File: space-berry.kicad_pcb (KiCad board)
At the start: 8 copper layers, 128 parts, among them Q1 SiS415DNT, Q2 TSM2302CX, U11 RTL8211F-CG, U12 K4A8G165WC-BCTD, U13 XCZU15EG-2FFVB1156E, U14 K4A8G165WC-BCTD, U6 TLV75801PDBV, U7 TLV75801PDBV, U8 TLV75801PDBV, U9 TLV75801PDBV

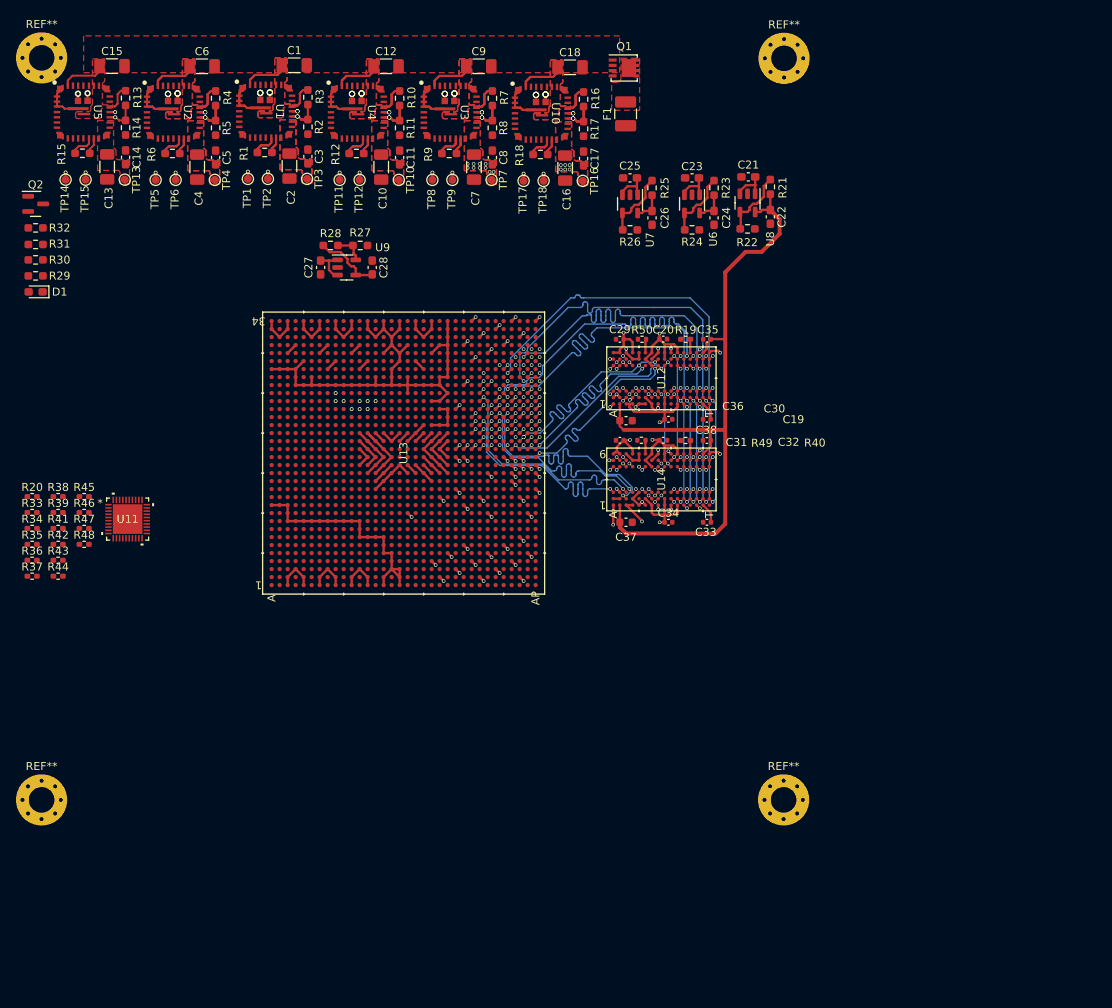
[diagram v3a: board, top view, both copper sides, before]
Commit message: Gbe routing
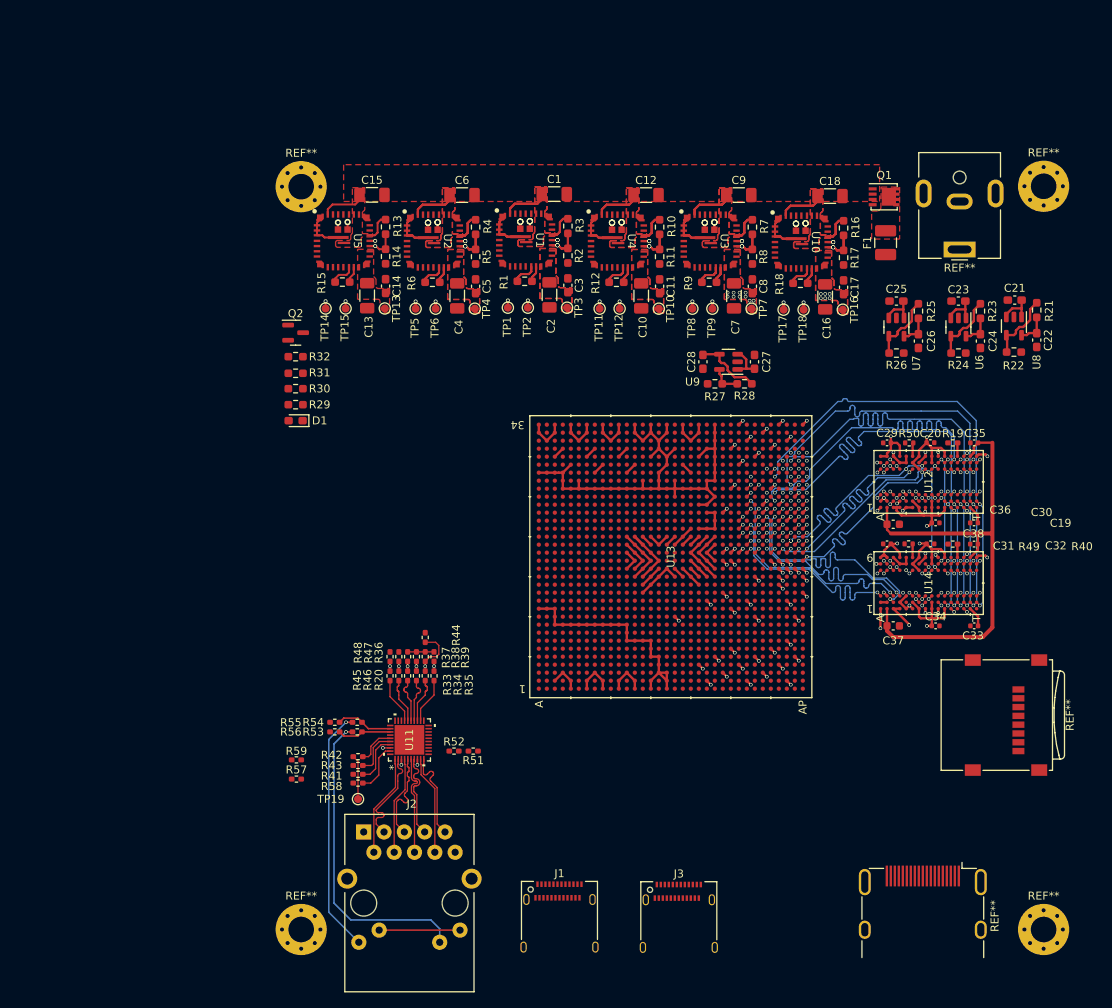
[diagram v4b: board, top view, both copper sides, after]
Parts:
- added J1: USB_C_Receptacle, Connector_USB:USB_C_Receptacle_Amphenol_12401610E4-2A, F.Cu at (127.5, 140.1)
- added J2: RJ45_RB1-125B8G1A, Connector_RJ:RJ45_UDE_RB1-125B8G1A, F.Cu at (103.0, 128.5)
- added J3: USB_C_Receptacle, Connector_USB:USB_C_Receptacle_Amphenol_12401610E4-2A, F.Cu at (142.4, 140.1)
- added R51: 22, Resistor_SMD:R_0402_1005Metric_Pad0.72x0.64mm_HandSolder, F.Cu at (116.7, 118.4)
- added R52: 4K7, Resistor_SMD:R_0402_1005Metric_Pad0.72x0.64mm_HandSolder, F.Cu at (114.3, 118.4)
- added R53: 420, Resistor_SMD:R_0402_1005Metric_Pad0.72x0.64mm_HandSolder, F.Cu at (102.2, 116.0)
- added R54: 420, Resistor_SMD:R_0402_1005Metric_Pad0.72x0.64mm_HandSolder, F.Cu at (102.2, 114.8)
- added R55: 4K7, Resistor_SMD:R_0402_1005Metric_Pad0.72x0.64mm_HandSolder, F.Cu at (99.4, 114.8)
- added R56: 4K7, Resistor_SMD:R_0402_1005Metric_Pad0.72x0.64mm_HandSolder, F.Cu at (99.4, 116.0)
- added R57: 420, Resistor_SMD:R_0402_1005Metric_Pad0.72x0.64mm_HandSolder, F.Cu at (94.6, 121.9)
- added R58: 2K5, Resistor_SMD:R_0402_1005Metric_Pad0.72x0.64mm_HandSolder, F.Cu at (102.3, 122.4)
- added R59: 4K7, Resistor_SMD:R_0402_1005Metric_Pad0.72x0.64mm_HandSolder, F.Cu at (94.6, 119.5)
- added REF**: BarrelJack_CUI_PJ-063AH_Horizontal, Connector_BarrelJack:BarrelJack_CUI_PJ-063AH_Horizontal, F.Cu at (177.5, 55.7)
- added REF**: HDMI_A_Molex_208658-1001_Horizontal, Connector_HDMI:HDMI_A_Molex_208658-1001_Horizontal, F.Cu at (172.9, 137.3)
- added REF**: microSD_HC_Wuerth_693072010801, Connector_Card:microSD_HC_Wuerth_693072010801, F.Cu at (183.3, 113.9)
- added TP19: Eth clk, TestPoint:TestPoint_Pad_D1.0mm, F.Cu at (102.3, 124.4)
- R41, R42, R43: value 4K7 -> 22
- R44: value 4K7 -> 1K
- R47, R48: value 22 -> 1K
- moved C27 55.5 mm to (151.9, 69.7), turned to 90 degrees
- moved R28 54.6 mm to (150.6, 72.5), turned to 0 degrees
- moved R35 52.9 mm to (111.8, 109.0), turned to -90 degrees
- moved R34 52.5 mm to (110.7, 109.0), turned to -90 degrees
- moved R33 52.2 mm to (109.6, 109.0), turned to -90 degrees
- moved R20 52.0 mm to (108.5, 109.0), turned to -90 degrees
- moved R36 51.7 mm to (111.8, 106.6), turned to -90 degrees
- moved R37 50.2 mm to (110.7, 106.6), turned to -90 degrees
- moved U9 49.2 mm to (148.6, 69.7), turned to 180 degrees
- moved R38 49.1 mm to (109.6, 106.6), turned to -90 degrees
- moved R41 48.5 mm to (102.3, 121.3), turned to 180 degrees
- moved R27 47.6 mm to (146.9, 72.5), turned to 0 degrees
- moved R39 47.3 mm to (108.5, 106.6), turned to -90 degrees
- moved R44 46.5 mm to (110.7, 104.2), turned to -90 degrees
- moved R42 45.9 mm to (102.3, 119.1), turned to 180 degrees
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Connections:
- R41 pad 1: 1V8_ETH -> Net-(U11A-XTAL_OUT/EXT_CLK)
- R41 pad 2: ETH_TXD3 -> ETH_CLK
- R42 pad 1: 1V8_ETH -> Net-(U11A-CLKOUT)
- R42 pad 2: ETH_TXD2 -> Net-(R42-Pad2)
- R43 pad 1: 1V8_ETH -> Net-(U11A-XTAL_IN)
- R43 pad 2: ETH_TXD1 -> GND
- R44 pad 1: 1V8_ETH -> GND
- R44 pad 2: ETH_TXD0 -> ETH_RXD2
- R45 pad 1: ETH_TXD0 -> Net-(U11A-RXC/PHYAD1)
- R45 pad 2: Net-(U11A-TXD0) -> ETH_RX_CTL
- R46 pad 1: ETH_TXD1 -> Net-(U11A-RXCTL/PHYAD2)
- R46 pad 2: Net-(U11A-TXD1) -> ETH_RX_CLK
- R47 pad 1: ETH_TXD2 -> GND
- R47 pad 2: Net-(U11A-TXD2) -> ETH_RX_CLK
- R48 pad 1: ETH_TXD3 -> GND
- R48 pad 2: Net-(U11A-TXD3) -> ETH_RX_CTL
- U11 pad 11: (no net) -> 3V3
- U11 pad 12: unconnected-(U11A-PHYRSTB-Pad12) -> Net-(U11A-PHYRSTB)
- U11 pad 15: Net-(U11A-TXD3) -> ETH_TXD3
- U11 pad 16: Net-(U11A-TXD2) -> ETH_TXD2
- U11 pad 17: Net-(U11A-TXD1) -> ETH_TXD1
- U11 pad 18: Net-(U11A-TXD0) -> ETH_TXD0
- U11 pad 19: unconnected-(U11A-TXCTL-Pad19) -> ETH_TX_CTL
- U11 pad 20: unconnected-(U11A-TXC-Pad20) -> ETH_TX_CLK
- U11 pad 21: (no net) -> unconnected-(U11B-DVDD10-Pad21)
- U11 pad 26: unconnected-(U11A-RXCTL/PHYAD2-Pad26) -> Net-(U11A-RXCTL/PHYAD2)
- U11 pad 27: unconnected-(U11A-RXC/PHYAD1-Pad27) -> Net-(U11A-RXC/PHYAD1)
- U11 pad 28: (no net) -> unconnected-(U11B-DVDD_RG-Pad28)
- U11 pad 29: (no net) -> unconnected-(U11B-DVDD33-Pad29)
- U11 pad 3: (no net) -> Net-(U11B-AVDD10-Pad3)
- U11 pad 32: unconnected-(U11A-LED0/CFG_EXT-Pad32) -> ETH_LED_G
- U11 pad 33: unconnected-(U11A-LED1/CFG_LDO0-Pad33) -> ETH_LED_Y
- U11 pad 34: unconnected-(U11A-LED2/CFG_LDO1-Pad34) -> Net-(D2-A)
- U11 pad 35: unconnected-(U11A-CLKOUT-Pad35) -> Net-(U11A-CLKOUT)
- U11 pad 36: unconnected-(U11A-XTAL_IN-Pad36) -> Net-(U11A-XTAL_IN)
- U11 pad 37: unconnected-(U11A-XTAL_OUT/EXT_CLK-Pad37) -> Net-(U11A-XTAL_OUT/EXT_CLK)
- U11 pad 38: (no net) -> Net-(U11B-AVDD10-Pad3)
- U11 pad 39: unconnected-(U11A-RSET-Pad39) -> Net-(U11A-RSET)
- U11 pad 40: (no net) -> 3V3
- U11 pad 41: (no net) -> GND
- U11 pad 8: (no net) -> Net-(U11B-AVDD10-Pad3)
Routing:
- net Net-(J2-PadL2): track 0.00 -> 39.1 mm, vias 0 -> 1
- net Net-(J2-PadL4): track 0.00 -> 30.7 mm, vias 0 -> 1
- net 2V5_LDO: track 87.6 -> 67.0 mm
- net ETH_TR1+: track 0.00 -> 12.8 mm
- net ETH_TR3+: track 0.00 -> 12.8 mm
- net ETH_TR1-: track 0.00 -> 12.7 mm
- net ETH_TR4+: track 0.00 -> 12.4 mm
- net ETH_TR2+: track 0.00 -> 12.2 mm
- net ETH_TR2-: track 0.00 -> 12.0 mm
- net ETH_TR4-: track 0.00 -> 11.7 mm
- net ETH_TR3-: track 0.00 -> 11.3 mm
- net Net-(J2-PadL1): track 0.00 -> 10.1 mm
- net ETH_LED_G: track 0.00 -> 7.09 mm
- net ETH_LED_Y: track 0.00 -> 6.76 mm
- net Net-(U11A-RSET): track 0.00 -> 6.35 mm
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- removed copper zone on In3.Cu, net 1V2

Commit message: usb and stuff
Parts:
- removed the REF** at (183.3, 113.9)
- added C39: 100nF, Capacitor_SMD:C_0402_1005Metric_Pad0.74x0.62mm_HandSolder, F.Cu at (140.8, 125.1)
- added C40: 100nF, Capacitor_SMD:C_0402_1005Metric_Pad0.74x0.62mm_HandSolder, F.Cu at (124.8, 125.1)
- added C41: 100nF, Capacitor_SMD:C_0402_1005Metric_Pad0.74x0.62mm_HandSolder, F.Cu at (149.5, 124.6)
- added C42: 100nF, Capacitor_SMD:C_0402_1005Metric_Pad0.74x0.62mm_HandSolder, F.Cu at (133.5, 124.6)
- added C43: 100nF, Capacitor_SMD:C_0402_1005Metric_Pad0.74x0.62mm_HandSolder, F.Cu at (146.8, 133.6)
- added C44: 100nF, Capacitor_SMD:C_0402_1005Metric_Pad0.74x0.62mm_HandSolder, F.Cu at (130.8, 133.6)
- added C45: 100nF, Capacitor_SMD:C_0402_1005Metric_Pad0.74x0.62mm_HandSolder, F.Cu at (140.8, 132.6)
- added C46: 100nF, Capacitor_SMD:C_0402_1005Metric_Pad0.74x0.62mm_HandSolder, F.Cu at (124.8, 132.6)
- added C47: 100nF, Capacitor_SMD:C_0402_1005Metric_Pad0.74x0.62mm_HandSolder, F.Cu at (138.0, 128.9)
- added C48: 100nF, Capacitor_SMD:C_0402_1005Metric_Pad0.74x0.62mm_HandSolder, F.Cu at (150.5, 124.6)
- added C49: 100nF, Capacitor_SMD:C_0402_1005Metric_Pad0.74x0.62mm_HandSolder, F.Cu at (140.8, 126.2)
- added C50: 100nF, Capacitor_SMD:C_0402_1005Metric_Pad0.74x0.62mm_HandSolder, F.Cu at (140.8, 131.5)
- added C51: 100nF, Capacitor_SMD:C_0402_1005Metric_Pad0.74x0.62mm_HandSolder, F.Cu at (122.0, 128.9)
- added C52: 100nF, Capacitor_SMD:C_0402_1005Metric_Pad0.74x0.62mm_HandSolder, F.Cu at (134.5, 124.6)
- added C53: 100nF, Capacitor_SMD:C_0402_1005Metric_Pad0.74x0.62mm_HandSolder, F.Cu at (124.8, 126.2)
- added C54: 100nF, Capacitor_SMD:C_0402_1005Metric_Pad0.74x0.62mm_HandSolder, F.Cu at (124.8, 131.5)
- added G***: LOGO, LOGO, F.Cu at (167.1, 119.4)
- added R60: R, Resistor_SMD:R_0402_1005Metric_Pad0.72x0.64mm_HandSolder, F.Cu at (142.2, 133.5)
- added R61: R, Resistor_SMD:R_0402_1005Metric_Pad0.72x0.64mm_HandSolder, F.Cu at (126.2, 133.5)
- added R62: R, Resistor_SMD:R_0402_1005Metric_Pad0.72x0.64mm_HandSolder, F.Cu at (144.4, 133.6)
- added R63: R, Resistor_SMD:R_0402_1005Metric_Pad0.72x0.64mm_HandSolder, F.Cu at (128.4, 133.6)
- added R64: R, Resistor_SMD:R_0402_1005Metric_Pad0.72x0.64mm_HandSolder, F.Cu at (138.0, 132.0)
- added R65: R, Resistor_SMD:R_0402_1005Metric_Pad0.72x0.64mm_HandSolder, F.Cu at (122.0, 132.0)
- added REF**: PinHeader_2x07_P2.54mm_Vertical, Connector_PinHeader_2.54mm:PinHeader_2x07_P2.54mm_Vertical, F.Cu at (185.7, 82.6)
- added REF**: Oscillator_SMD_EuroQuartz_XO32-4Pin_3.2x2.5mm, Oscillator:Oscillator_SMD_EuroQuartz_XO32-4Pin_3.2x2.5mm, F.Cu at (95.0, 126.6)
- added REF**: PinSocket_2x10_P2.54mm_Vertical, Connector_PinSocket_2.54mm:PinSocket_2x10_P2.54mm_Vertical, F.Cu at (97.5, 84.6)
- added REF**: SW_DIP_SPSTx04_Slide_6.7x11.72mm_W8.61mm_P2.54mm_LowProfile, Button_Switch_SMD:SW_DIP_SPSTx04_Slide_6.7x11.72mm_W8.61mm_P2.54mm_LowProfile, F.Cu at (183.9, 120.2)
- added U15: USB3300-EZK, Package_DFN_QFN:QFN-32-1EP_5x5mm_P0.5mm_EP3.45x3.45mm, F.Cu at (147.0, 129.3)
- added U16: USB3300-EZK, Package_DFN_QFN:QFN-32-1EP_5x5mm_P0.5mm_EP3.45x3.45mm, F.Cu at (131.0, 129.3)
- added U17: CDCI6214RGET, lib:CDCI6214RGET_NV, F.Cu at (110.2, 87.8)
- added X1: ECS-2520MV-xxx-xx, Oscillator:Oscillator_SMD_ECS_2520MV-xxx-xx-4Pin_2.5x2.0mm, F.Cu at (140.8, 128.9)
- added X2: ECS-2520MV-xxx-xx, Oscillator:Oscillator_SMD_ECS_2520MV-xxx-xx-4Pin_2.5x2.0mm, F.Cu at (124.8, 128.9)
- J1, J3: value USB_C_Receptacle -> USB_C_Receptacle_USB2.0; footprint Connector_USB:USB_C_Receptacle_Amphenol_12401610E4-2A -> Connector_USB:USB_C_Receptacle_G-Switch_GT-USB-7010ASV
- moved C27 12.4 mm to (139.4, 69.8)
- moved R28 12.4 mm to (138.2, 72.5)
- moved U9 12.4 mm to (136.2, 69.8)
- moved C28 12.4 mm to (133.0, 69.8)
- moved R27 12.4 mm to (134.5, 72.5)
- moved REF** 6.40 mm to (166.5, 137.3)
- moved J3 3.31 mm to (145.3, 141.7)
- moved R51 2.64 mm to (114.3, 119.5)
- moved J1 2.45 mm to (129.3, 141.7)
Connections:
- J1 pad A1: Net-(J1-GND-PadA1) -> GND
- J1 pad A12: Net-(J1-GND-PadA1) -> GND
- J1 pad A4: Net-(J1-VBUS-PadA4) -> 5V0
- J1 pad A6: unconnected-(J1-D+-PadA6) -> /USB_2_2/USB0_D+
- J1 pad A7: unconnected-(J1-D--PadA7) -> /USB_2_2/USB0_D-
- J1 pad A9: Net-(J1-VBUS-PadA4) -> 5V0
- J1 pad B1: Net-(J1-GND-PadA1) -> GND
- J1 pad B12: Net-(J1-GND-PadA1) -> GND
- J1 pad B4: Net-(J1-VBUS-PadA4) -> 5V0
- J1 pad B6: unconnected-(J1-D+-PadB6) -> /USB_2_2/USB0_D+
- J1 pad B7: unconnected-(J1-D--PadB7) -> /USB_2_2/USB0_D-
- J1 pad B9: Net-(J1-VBUS-PadA4) -> 5V0
- J1 pad S1: unconnected-(J1-SHIELD-PadS1) -> GND
- J3 pad A1: Net-(J3-GND-PadA1) -> GND
- J3 pad A12: Net-(J3-GND-PadA1) -> GND
- J3 pad A4: Net-(J3-VBUS-PadA4) -> 5V0
- J3 pad A6: unconnected-(J3-D+-PadA6) -> /USB_2.0/USB0_D+
- J3 pad A7: unconnected-(J3-D--PadA7) -> /USB_2.0/USB0_D-
- J3 pad A9: Net-(J3-VBUS-PadA4) -> 5V0
- J3 pad B1: Net-(J3-GND-PadA1) -> GND
- J3 pad B12: Net-(J3-GND-PadA1) -> GND
- J3 pad B4: Net-(J3-VBUS-PadA4) -> 5V0
- J3 pad B6: unconnected-(J3-D+-PadB6) -> /USB_2.0/USB0_D+
- J3 pad B7: unconnected-(J3-D--PadB7) -> /USB_2.0/USB0_D-
- J3 pad B9: Net-(J3-VBUS-PadA4) -> 5V0
- J3 pad S1: unconnected-(J3-SHIELD-PadS1) -> GND
- U13 pad A23: (no net) -> USB0_DATA_1
- U13 pad A25: (no net) -> USB1_DATA_CLK_O
- U13 pad A26: (no net) -> USB1_DATA_DIR
- U13 pad A27: (no net) -> USB1_DATA_2
- U13 pad A3: (no net) -> unconnected-(U13A-MGTHRXN3_230-PadA3)
- U13 pad A31: (no net) -> unconnected-(U13A-MGTHTXP3_130-PadA31)
- U13 pad A32: (no net) -> unconnected-(U13A-MGTHTXN3_130-PadA32)
- U13 pad A4: (no net) -> unconnected-(U13A-MGTHRXP3_230-PadA4)
- U13 pad A7: (no net) -> unconnected-(U13A-MGTHTXN3_230-PadA7)
- U13 pad A8: (no net) -> unconnected-(U13A-MGTHTXP3_230-PadA8)
- U13 pad B1: (no net) -> unconnected-(U13A-MGTHRXN2_230-PadB1)
- U13 pad B2: (no net) -> unconnected-(U13A-MGTHRXP2_230-PadB2)
- U13 pad B23: (no net) -> USB0_DATA_NXT
- U13 pad B24: (no net) -> USB0_DATA_3
- U13 pad B25: (no net) -> USB1_DATA_NXT
- U13 pad B26: (no net) -> USB1_DATA_0
- U13 pad B27: (no net) -> USB1_DATA_1
- U13 pad B29: (no net) -> unconnected-(U13A-MGTHTXP2_130-PadB29)
- U13 pad B30: (no net) -> unconnected-(U13A-MGTHTXN2_130-PadB30)
- U13 pad B33: (no net) -> unconnected-(U13A-MGTHRXP3_130-PadB33)
- U13 pad B34: (no net) -> unconnected-(U13A-MGTHRXN3_130-PadB34)
- U13 pad B5: (no net) -> unconnected-(U13A-MGTHTXN2_230-PadB5)
- U13 pad B6: (no net) -> unconnected-(U13A-MGTHTXP2_230-PadB6)
- U13 pad C23: (no net) -> USB0_DATA_0
- U13 pad C24: (no net) -> USB0_DATA_5
- U13 pad C26: (no net) -> USB1_DATA_STP
- U13 pad C27: (no net) -> USB1_DATA_3
- U13 pad C3: (no net) -> unconnected-(U13A-MGTHRXN1_230-PadC3)
- U13 pad C31: (no net) -> unconnected-(U13A-MGTHRXP2_130-PadC31)
- U13 pad C32: (no net) -> unconnected-(U13A-MGTHRXN2_130-PadC32)
- U13 pad C4: (no net) -> unconnected-(U13A-MGTHRXP1_230-PadC4)
- U13 pad D1: (no net) -> unconnected-(U13A-MGTHRXN0_230-PadD1)
- U13 pad D2: (no net) -> unconnected-(U13A-MGTHRXP0_230-PadD2)
- U13 pad D24: (no net) -> USB0_DATA_8
- U13 pad D25: (no net) -> USB1_DATA_8
- U13 pad D29: (no net) -> unconnected-(U13A-MGTHTXP1_130-PadD29)
- U13 pad D30: (no net) -> unconnected-(U13A-MGTHTXN1_130-PadD30)
- U13 pad D33: (no net) -> unconnected-(U13A-MGTHRXP1_130-PadD33)
- U13 pad D34: (no net) -> unconnected-(U13A-MGTHRXN1_130-PadD34)
- U13 pad D5: (no net) -> unconnected-(U13A-MGTHTXN1_230-PadD5)
- U13 pad D6: (no net) -> unconnected-(U13A-MGTHTXP1_230-PadD6)
- U13 pad E23: unconnected-(U13K-PS_MIO53-PadE23) -> USB0_DATA_DIR
- U13 pad E24: (no net) -> USB0_DATA_4
- U13 pad E25: (no net) -> USB1_DATA_4
- U13 pad E3: (no net) -> unconnected-(U13A-MGTHTXN0_230-PadE3)
- U13 pad E31: (no net) -> unconnected-(U13A-MGTHRXP0_130-PadE31)
- U13 pad E32: (no net) -> unconnected-(U13A-MGTHRXN0_130-PadE32)
- U13 pad E4: (no net) -> unconnected-(U13A-MGTHTXP0_230-PadE4)
- U13 pad F1: (no net) -> unconnected-(U13A-MGTHRXN3_229-PadF1)
- U13 pad F2: (no net) -> unconnected-(U13A-MGTHRXP3_229-PadF2)
- U13 pad F22: unconnected-(U13K-PS_MIO52-PadF22) -> USB0_DATA_CLK_O
- U13 pad F23: (no net) -> USB0_DATA_2
- U13 pad F25: (no net) -> unconnected-(U13L-PS_MIO77-PadF25)
- U13 pad F29: (no net) -> unconnected-(U13A-MGTHTXP0_130-PadF29)
- U13 pad F30: (no net) -> unconnected-(U13A-MGTHTXN0_130-PadF30)
- U13 pad F33: (no net) -> unconnected-(U13A-MGTHRXP3_129-PadF33)
- U13 pad F34: (no net) -> unconnected-(U13A-MGTHRXN3_129-PadF34)
- U13 pad F5: (no net) -> unconnected-(U13A-MGTHTXN3_229-PadF5)
- U13 pad F6: (no net) -> unconnected-(U13A-MGTHTXP3_229-PadF6)
- U13 pad G23: (no net) -> USB0_DATA_STP
- U13 pad G24: (no net) -> USB0_DATA_6
- U13 pad G25: (no net) -> USB1_DATA_6
- U13 pad G3: (no net) -> unconnected-(U13A-MGTHTXN2_229-PadG3)
- U13 pad G31: (no net) -> unconnected-(U13A-MGTHTXP3_129-PadG31)
- U13 pad G32: (no net) -> unconnected-(U13A-MGTHTXN3_129-PadG32)
- U13 pad G4: (no net) -> unconnected-(U13A-MGTHTXP2_229-PadG4)
- U13 pad H1: (no net) -> unconnected-(U13A-MGTHRXN2_229-PadH1)
- U13 pad H2: (no net) -> unconnected-(U13A-MGTHRXP2_229-PadH2)
- U13 pad H24: (no net) -> USB1_DATA_5
- U13 pad H25: (no net) -> unconnected-(U13L-PS_MIO76-PadH25)
- U13 pad H29: (no net) -> unconnected-(U13A-MGTHTXP2_129-PadH29)
- U13 pad H30: (no net) -> unconnected-(U13A-MGTHTXN2_129-PadH30)
- U13 pad H33: (no net) -> unconnected-(U13A-MGTHRXP2_129-PadH33)
- U13 pad H34: (no net) -> unconnected-(U13A-MGTHRXN2_129-PadH34)
- U13 pad H5: (no net) -> unconnected-(U13A-MGTHTXN1_229-PadH5)
- U13 pad H6: (no net) -> unconnected-(U13A-MGTHTXP1_229-PadH6)
- U13 pad J3: (no net) -> unconnected-(U13A-MGTHRXN1_229-PadJ3)
- U13 pad J31: (no net) -> unconnected-(U13A-MGTHTXP1_129-PadJ31)
- U13 pad J32: (no net) -> unconnected-(U13A-MGTHTXN1_129-PadJ32)
- U13 pad J4: (no net) -> unconnected-(U13A-MGTHRXP1_229-PadJ4)
- U13 pad K1: (no net) -> unconnected-(U13A-MGTHRXN0_229-PadK1)
- U13 pad K2: (no net) -> unconnected-(U13A-MGTHRXP0_229-PadK2)
- U13 pad K29: (no net) -> unconnected-(U13A-MGTHTXP0_129-PadK29)
- U13 pad K30: (no net) -> unconnected-(U13A-MGTHTXN0_129-PadK30)
- U13 pad K33: (no net) -> unconnected-(U13A-MGTHRXP1_129-PadK33)
- U13 pad K34: (no net) -> unconnected-(U13A-MGTHRXN1_129-PadK34)
- U13 pad K5: (no net) -> unconnected-(U13A-MGTHTXN0_229-PadK5)
- U13 pad K6: (no net) -> unconnected-(U13A-MGTHTXP0_229-PadK6)
- U13 pad L3: (no net) -> unconnected-(U13A-MGTHRXN3_228-PadL3)
- U13 pad L31: (no net) -> unconnected-(U13A-MGTHRXP0_129-PadL31)
- U13 pad L32: (no net) -> unconnected-(U13A-MGTHRXN0_129-PadL32)
- U13 pad L4: (no net) -> unconnected-(U13A-MGTHRXP3_228-PadL4)
- U13 pad M1: (no net) -> unconnected-(U13A-MGTHRXN2_228-PadM1)
- U13 pad M2: (no net) -> unconnected-(U13A-MGTHRXP2_228-PadM2)
- U13 pad M29: (no net) -> unconnected-(U13A-MGTHTXP3_128-PadM29)
- U13 pad M30: (no net) -> unconnected-(U13A-MGTHTXN3_128-PadM30)
- U13 pad M33: (no net) -> unconnected-(U13A-MGTHRXP3_128-PadM33)
- U13 pad M34: (no net) -> unconnected-(U13A-MGTHRXN3_128-PadM34)
- U13 pad M5: (no net) -> unconnected-(U13A-MGTHTXN3_228-PadM5)
- U13 pad M6: (no net) -> unconnected-(U13A-MGTHTXP3_228-PadM6)
- U13 pad N3: (no net) -> unconnected-(U13A-MGTHTXN2_228-PadN3)
- U13 pad N31: (no net) -> unconnected-(U13A-MGTHRXP2_128-PadN31)
- U13 pad N32: (no net) -> unconnected-(U13A-MGTHRXN2_128-PadN32)
- U13 pad N4: (no net) -> unconnected-(U13A-MGTHTXP2_228-PadN4)
- U13 pad P1: (no net) -> DP_L2_RX-
- U13 pad P2: (no net) -> DP_L2_RX+
- U13 pad P29: (no net) -> unconnected-(U13A-MGTHTXP2_128-PadP29)
- U13 pad P30: (no net) -> unconnected-(U13A-MGTHTXN2_128-PadP30)
- U13 pad P33: (no net) -> unconnected-(U13A-MGTHRXP1_128-PadP33)
- U13 pad P34: (no net) -> unconnected-(U13A-MGTHRXN1_128-PadP34)
- U13 pad P5: (no net) -> DP_L2_TX-
- U13 pad P6: (no net) -> DP_L2_TX+
- U13 pad R22: (no net) -> unconnected-(U13L-PS_MODE1-PadR22)
- U13 pad R23: (no net) -> unconnected-(U13L-PS_MODE3-PadR23)
- U13 pad R3: (no net) -> DP_L1_TX-
- U13 pad R31: (no net) -> unconnected-(U13A-MGTHTXP1_128-PadR31)
- U13 pad R32: (no net) -> unconnected-(U13A-MGTHTXN1_128-PadR32)
- U13 pad R4: (no net) -> DP_L1_TX+
- U13 pad T1: (no net) -> DP_L1_RX-
- U13 pad T2: (no net) -> DP_L1_RX+
- U13 pad T22: (no net) -> unconnected-(U13L-PS_MODE0-PadT22)
- U13 pad T23: (no net) -> unconnected-(U13L-PS_MODE2-PadT23)
- U13 pad T29: (no net) -> unconnected-(U13A-MGTHTXP0_128-PadT29)
- U13 pad T30: (no net) -> unconnected-(U13A-MGTHTXN0_128-PadT30)
- U13 pad T33: (no net) -> unconnected-(U13A-MGTHRXP0_128-PadT33)
- U13 pad T34: (no net) -> unconnected-(U13A-MGTHRXN0_128-PadT34)
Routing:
- net GND: track 240.3 -> 146.4 mm, vias 87 -> 159
- net 3V3: track 13.0 -> 74.0 mm, vias 0 -> 8
- net 1V8: track 4.10 -> 59.0 mm, vias 0 -> 8
- net /USB_2_2/USB0_D-: track 0.00 -> 23.9 mm, vias 0 -> 4
- net /USB_2.0/USB0_D-: track 0.00 -> 23.9 mm, vias 0 -> 4
- net /USB_2.0/USB0_D+: track 0.00 -> 23.9 mm, vias 0 -> 4
- net /USB_2_2/USB0_D+: track 0.00 -> 23.9 mm, vias 0 -> 4
- net DP_L2_TX-: track 0.00 -> 7.58 mm, vias 0 -> 1
- net DP_L2_TX+: track 0.00 -> 7.58 mm, vias 0 -> 1
- net DP_L1_TX-: track 0.00 -> 7.01 mm, vias 0 -> 1
- net DP_L1_TX+: track 0.00 -> 7.01 mm, vias 0 -> 1
- net Net-(U16-VBUS): track 0.00 -> 6.56 mm
- net Net-(U15-VBUS): track 0.00 -> 6.56 mm
- net Net-(U16-RBIAS): track 0.00 -> 6.53 mm
- net Net-(U15-RBIAS): track 0.00 -> 6.53 mm
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
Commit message: stuff
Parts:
- removed J1, J3: USB_C_Receptacle_USB2.0, Connector_USB:USB_C_Receptacle_G-Switch_GT-USB-7010ASV
- removed the REF** at (95.0, 126.6)
- added D2: LED, LED_SMD:LED_0603_1608Metric_Pad1.05x0.95mm_HandSolder, F.Cu at (101.9, 117.4)
- added REF**: 48406-0003_MOL, lib:48406-0003_MOL, F.Cu at (128.7, 132.6)
- added REF**: CONN9_08-0003_MOL, lib:CONN9_08-0003_MOL, F.Cu at (106.6, 69.9)
- added REF**: CONN_67800-8025_MOL, lib:CONN_67800-8025_MOL, F.Cu at (135.8, 120.1)
- C39, C40, C41, C42, C43, C44, C45, C46, C47, C49, C50, C51, C52, C54, R41, R42, R43, R51, R52, R53, R54, R55, R56, R58, R60, R61, R62, R63: moved to B.Cu
- U13: footprint lib:FFVB1156_XIL-L -> lib:FFVB1156_XIL
- moved R61 57.9 mm to (106.7, 79.0), turned to -90 degrees
- moved U17 57.4 mm to (152.5, 126.5)
- moved R62 56.0 mm to (104.4, 94.4)
- moved R63 56.0 mm to (104.4, 83.0)
- moved R60 55.9 mm to (106.8, 90.2), turned to -90 degrees
- moved C54 54.8 mm to (109.1, 79.0), turned to 90 degrees
- moved R65 53.5 mm to (117.4, 78.7)
- moved C45 53.5 mm to (108.1, 90.2), turned to 90 degrees
- moved C46 52.7 mm to (104.4, 84.0)
- moved C50 52.0 mm to (109.1, 90.2), turned to 90 degrees
- moved X2 51.2 mm to (115.2, 78.7), turned to -90 degrees
- moved C51 51.1 mm to (111.1, 79.0), turned to 90 degrees
- moved U15 51.1 mm to (109.4, 94.7), turned to 0 degrees
- moved C41 50.7 mm to (112.1, 90.2), turned to -90 degrees
- moved U16 50.7 mm to (109.4, 83.3), turned to 0 degrees
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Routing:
- net 3V3: track 74.0 -> 13.0 mm, vias 8 -> 7
- net 1V8: track 59.0 -> 4.10 mm, vias 8 -> 6
- net Net-(J2-PadL2): track 39.1 -> 0.00 mm, vias 1 -> 0
- net Net-(J2-PadL4): track 30.7 -> 0.00 mm, vias 1 -> 0
- net /USB_2_2/USB0_D-: track 23.9 -> 2.70 mm, vias 4 -> 0
- net /USB_2.0/USB0_D-: track 23.9 -> 2.70 mm, vias 4 -> 0
- net /USB_2.0/USB0_D+: track 23.9 -> 2.67 mm, vias 4 -> 0
- net /USB_2_2/USB0_D+: track 23.9 -> 2.67 mm, vias 4 -> 0
- net ETH_LED_G: track 7.09 -> 0.00 mm, vias 0 -> 1
- net DP_L2_TX-: track 7.58 -> 0.71 mm
- net DP_L2_TX+: track 7.58 -> 0.71 mm
- net ETH_LED_Y: track 6.76 -> 0.00 mm, vias 0 -> 1
- net Net-(U16-VBUS): track 6.56 -> 0.00 mm, vias 0 -> 1
- net Net-(U15-VBUS): track 6.56 -> 0.00 mm, vias 0 -> 1
- net Net-(U16-RBIAS): track 6.53 -> 0.00 mm, vias 0 -> 1
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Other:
- board outline added: 100 x 100 mm

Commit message: a.
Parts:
- added REF**: microSD_HC_Wuerth_693072010801, Connector_Card:microSD_HC_Wuerth_693072010801, F.Cu at (153.9, 136.7)
- added REF**: PinSocket_1x04_P2.54mm_Vertical, Connector_PinSocket_2.54mm:PinSocket_1x04_P2.54mm_Vertical, F.Cu at (96.6, 84.2)
- moved REF** 92.6 mm to (188.3, 102.7)
- moved U17 61.4 mm to (97.0, 100.2)
- moved REF** 29.9 mm to (154.0, 120.4), turned to 90 degrees
- moved R27 9.87 mm to (155.7, 71.2), turned to 90 degrees
- moved C28 9.36 mm to (152.9, 72.7), turned to 180 degrees
- moved R28 7.48 mm to (155.7, 67.5), turned to 90 degrees
- moved G*** 6.71 mm to (173.1, 116.4)
- moved U9 5.42 mm to (152.9, 69.5), turned to -90 degrees
- moved C27 3.49 mm to (152.9, 66.2), turned to 180 degrees
- moved REF** 2.48 mm to (173.7, 135.7)
- moved REF** 1.27 mm to (136.2, 118.9)
- moved C47 1.01 mm to (109.9, 99.1)
- moved C43 1.01 mm to (112.2, 99.1)
- moved R51 1.00 mm to (113.5, 118.2)
- moved R52 1.00 mm to (113.5, 119.2)
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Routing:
- net GND: track 146.4 -> 250.4 mm, vias 160 -> 200
- net /USB_2_2/USB0_D+: track 2.67 -> 68.7 mm
- net /USB_2_2/USB0_D-: track 2.70 -> 68.2 mm
- net DP_L1_TX-: track 0.71 -> 53.8 mm
- net DP_L1_TX+: track 0.71 -> 53.8 mm
- net DP_L2_TX-: track 0.71 -> 52.5 mm
- net DP_L2_TX+: track 0.71 -> 52.5 mm
- net /USB_2.0/USB0_D+: track 2.67 -> 54.4 mm
- net /USB_2.0/USB0_D-: track 2.70 -> 53.9 mm
- net DP_L1_RX-: track 0.71 -> 50.7 mm
- net DP_L1_RX+: track 0.71 -> 50.7 mm
- net ETH_TXD3: track 0.71 -> 48.9 mm, vias 1 -> 4
- net DP_L2_RX-: track 0.71 -> 48.7 mm
- net DP_L2_RX+: track 0.71 -> 48.7 mm
- net ETH_TXD2: track 0.71 -> 43.7 mm, vias 1 -> 2
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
